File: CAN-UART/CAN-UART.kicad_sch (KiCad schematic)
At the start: 15 parts, among them J1 Conn_01x06, P1 USB_C_Plug_USB2.0, U1 AP2112K-3.3, U2 SN65HVD230, U3 ESP32-C3, U4 AT45DB161D-SU

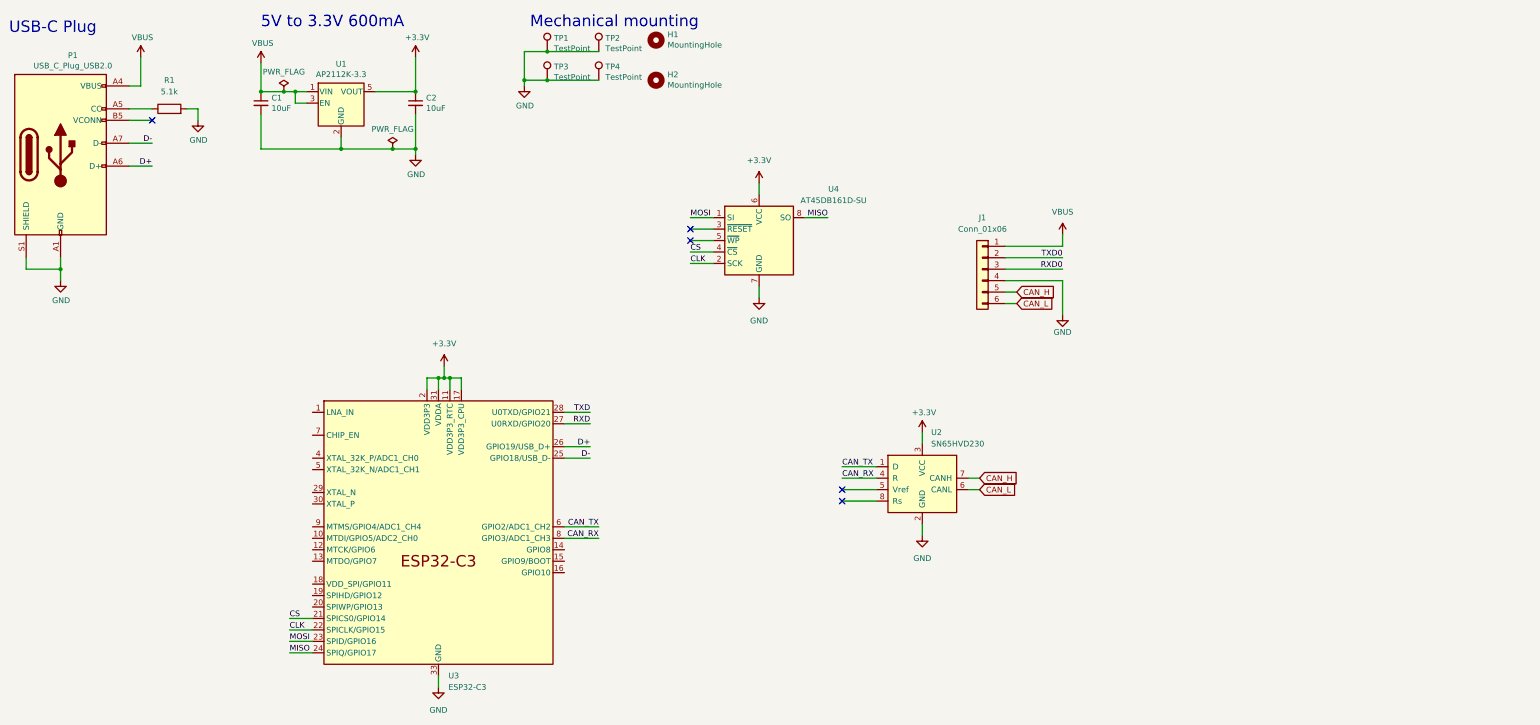
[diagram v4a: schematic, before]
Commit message: Added Power Cap
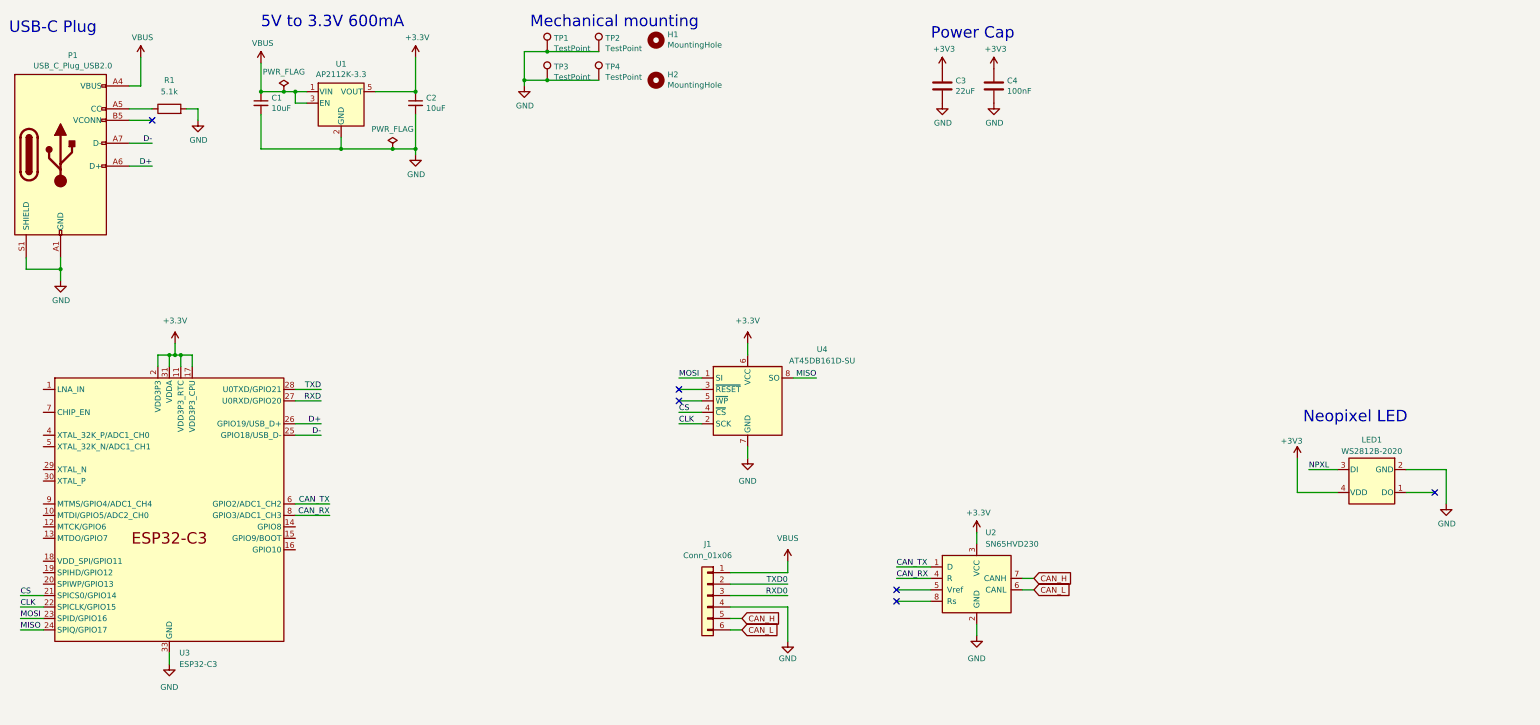
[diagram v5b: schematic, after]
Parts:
- added C3: 22uF, Capacitor_SMD:C_0402_1005Metric_Pad0.74x0.62mm_HandSolder, symbol Device:C
- added C4: 100nF, Capacitor_SMD:C_0402_1005Metric_Pad0.74x0.62mm_HandSolder, symbol Device:C
- added LED1: WS2812B-2020, _mykicadlib:LED-SMD_4P-L2.0-W2.0-TL_WS2812B-2020, symbol _mykicadlib:WS2812B-2020
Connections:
- net +3V3: now also C3.1, C4.1, LED1.4 (VDD)
- net GND: now also C3.2, C4.2, LED1.2 (GND)
- new net NPXL: LED1.3 (DI)
- no-connect marks 5 -> 6
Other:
- note added: "Neopixel LED"
- note added: "Power Cap"
- moved on the sheet: J1, U2, U3, U4

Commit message: Added NeoPixel LED
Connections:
- net NPXL: now also U3.14 (GPIO8)
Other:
- moved on the sheet: LED1
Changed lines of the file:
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@@
   (no_connect (at 57.15 39.37))
   (no_connect (at 173.99 99.06))
-  (no_connect (at 341.63 121.92))
+  (no_connect (at 254 109.22))
   (no_connect (at 222.25 143.51))
   (no_connect (at 173.99 101.6))
-  (wire (pts (xy 311.15 121.92) (xy 320.04 121.92))
+  (wire (pts (xy 223.52 109.22) (xy 232.41 109.22))
     (stroke (width 0) (type default))
   )
@@
     (stroke (width 0) (type default))
   )
-  (wire (pts (xy 341.63 121.92) (xy 335.28 121.92))
+  (wire (pts (xy 254 109.22) (xy 247.65 109.22))
     (stroke (width 0) (type default))
   )
@@
     (stroke (width 0) (type default))
   )
-  (wire (pts (xy 311.15 114.3) (xy 311.15 121.92))
+  (wire (pts (xy 223.52 101.6) (xy 223.52 109.22))
     (stroke (width 0) (type default))
   )
@@
     (stroke (width 0) (type default))
   )
-  (wire (pts (xy 313.69 116.84) (xy 320.04 116.84))
+  (wire (pts (xy 226.06 104.14) (xy 232.41 104.14))
     (stroke (width 0) (type default))
   )
@@
     (stroke (width 0) (type default))
   )
-  (wire (pts (xy 344.17 124.46) (xy 344.17 116.84))
+  (wire (pts (xy 256.54 111.76) (xy 256.54 104.14))
     (stroke (width 0) (type default))
   )
@@
     (stroke (width 0) (type default))
   )
-  (wire (pts (xy 335.28 116.84) (xy 344.17 116.84))
+  (wire (pts (xy 247.65 104.14) (xy 256.54 104.14))
+    (stroke (width 0) (type default))
+  )
+  (wire (pts (xy 96.52 129.54) (xy 88.9 129.54))
     (stroke (width 0) (type default))
   )
@@
     (effects (font (size 2.54 2.54)) (justify left bottom))
   )
-  (text "Neopixel LED" (at 312.42 106.68 0)
+  (text "Neopixel LED" (at 224.79 93.98 0)
     (effects (font (size 2.54 2.54)) (justify left bottom))
   )
@@
     (effects (font (size 1.27 1.27)) (justify right bottom))
   )
-  (label "NPXL" (at 313.69 116.84 0) (fields_autoplaced)
+  (label "NPXL" (at 226.06 104.14 0) (fields_autoplaced)
     (effects (font (size 1.27 1.27)) (justify left bottom))
   )
@@
   )
   (label "TXD" (at 94.615 99.06 180) (fields_autoplaced)
+    (effects (font (size 1.27 1.27)) (justify right bottom))
+  )
+  (label "NPXL" (at 96.52 129.54 180) (fields_autoplaced)
     (effects (font (size 1.27 1.27)) (justify right bottom))
   )
@@
     )
   )
-  (symbol (lib_id "_mykicadlib:WS2812B-2020") (at 327.66 119.38 0) (unit 1)
+  (symbol (lib_id "_mykicadlib:WS2812B-2020") (at 240.03 106.68 0) (unit 1)
     (in_bom yes) (on_board yes) (dnp no) (fields_autoplaced)
-    (property "Reference" "LED1" (at 327.66 110.236 0)
-      (effects (font (size 1.27 1.27)))
-    )
-    (property "Value" "WS2812B-2020" (at 327.66 112.776 0)
-      (effects (font (size 1.27 1.27)))
-    )
-    (property "Footprint" "_mykicadlib:LED-SMD_4P-L2.0-W2.0-TL_WS2812B-2020" (at 327.66 128.27 0)
-      (effects (font (size 1.27 1.27)) hide)
-    )
-    (property "Datasheet" "https://datasheet.lcsc.com/lcsc/2012110135_Worldsemi-WS2812B-2020_C965555.pdf" (at 327.66 130.81 0)
-      (effects (font (size 1.27 1.27)) hide)
-    )
-    (property "Manufacturer" "worldsemi" (at 327.66 133.35 0)
-      (effects (font (size 1.27 1.27)) hide)
-    )
-    (property "LCSC Part" "C965555" (at 327.66 135.89 0)
-      (effects (font (size 1.27 1.27)) hide)
-    )
-    (property "JLC Part" "Extended Part" (at 327.66 138.43 0)
-      (effects (font (size 1.27 1.27)) hide)
-    )
-    (property "LCSC#" "C965555" (at 334.01 130.81 0)
-      (effects (font (size 1.27 1.27)) hide)
-    )
-    (property "Part#" "WS2812B-2020" (at 336.55 133.35 0)
-      (effects (font (size 1.27 1.27)) hide)
-    )
-    (property "MPN" "C965555" (at 327.66 135.89 0)
+    (property "Reference" "LED1" (at 240.03 97.536 0)
+      (effects (font (size 1.27 1.27)))
+    )
+    (property "Value" "WS2812B-2020" (at 240.03 100.076 0)
+      (effects (font (size 1.27 1.27)))
+    )
+    (property "Footprint" "_mykicadlib:LED-SMD_4P-L2.0-W2.0-TL_WS2812B-2020" (at 240.03 115.57 0)
+      (effects (font (size 1.27 1.27)) hide)
+    )
+    (property "Datasheet" "https://datasheet.lcsc.com/lcsc/2012110135_Worldsemi-WS2812B-2020_C965555.pdf" (at 240.03 118.11 0)
+      (effects (font (size 1.27 1.27)) hide)
+    )
+    (property "Manufacturer" "worldsemi" (at 240.03 120.65 0)
+      (effects (font (size 1.27 1.27)) hide)
+    )
+    (property "LCSC Part" "C965555" (at 240.03 123.19 0)
+      (effects (font (size 1.27 1.27)) hide)
+    )
+    (property "JLC Part" "Extended Part" (at 240.03 125.73 0)
+      (effects (font (size 1.27 1.27)) hide)
+    )
+    (property "LCSC#" "C965555" (at 246.38 118.11 0)
+      (effects (font (size 1.27 1.27)) hide)
+    )
+    (property "Part#" "WS2812B-2020" (at 248.92 120.65 0)
+      (effects (font (size 1.27 1.27)) hide)
+    )
+    (property "MPN" "C965555" (at 240.03 123.19 0)
       (effects (font (size 1.27 1.27)) hide)
     )
@@
     )
   )
-  (symbol (lib_id "power:GND") (at 344.17 124.46 0) (unit 1)
-    (in_bom yes) (on_board yes) (dnp no)
-    (property "Reference" "#PWR020" (at 344.17 130.81 0)
-      (effects (font (size 1.27 1.27)) hide)
-    )
-    (property "Value" "GND" (at 344.297 128.8542 0)
-      (effects (font (size 1.27 1.27)))
-    )
-    (property "Footprint" "" (at 344.17 124.46 0)
-      (effects (font (size 1.27 1.27)) hide)
-    )
-    (property "Datasheet" "" (at 344.17 124.46 0)
+  (symbol (lib_id "power:GND") (at 256.54 111.76 0) (unit 1)
+    (in_bom yes) (on_board yes) (dnp no)
+    (property "Reference" "#PWR020" (at 256.54 118.11 0)
+      (effects (font (size 1.27 1.27)) hide)
+    )
+    (property "Value" "GND" (at 256.667 116.1542 0)
+      (effects (font (size 1.27 1.27)))
+    )
+    (property "Footprint" "" (at 256.54 111.76 0)
+      (effects (font (size 1.27 1.27)) hide)
+    )
+    (property "Datasheet" "" (at 256.54 111.76 0)
       (effects (font (size 1.27 1.27)) hide)
     )
@@
     )
   )
-  (symbol (lib_id "power:+3V3") (at 311.15 114.3 0) (unit 1)
-    (in_bom yes) (on_board yes) (dnp no)
-    (property "Reference" "#PWR019" (at 311.15 118.11 0)
-      (effects (font (size 1.27 1.27)) hide)
-    )
-    (property "Value" "+3V3" (at 309.88 110.49 0)
-      (effects (font (size 1.27 1.27)))
-    )
-    (property "Footprint" "" (at 311.15 114.3 0)
-      (effects (font (size 1.27 1.27)) hide)
-    )
-    (property "Datasheet" "" (at 311.15 114.3 0)
-      (effects (font (size 1.27 1.27)) hide)
-    )
+  (symbol (lib_id "power:+3V3") (at 223.52 101.6 0) (unit 1)
+    (in_bom yes) (on_board yes) (dnp no)
+    (property "Reference" "#PWR019" (at 223.52 105.41 0)
+      (effects (font (size 1.27 1.27)) hide)
+    )
+    (property "Value" "+3V3" (at 222.25 97.79 0)
+      (effects (font (size 1.27 1.27)))
+    )
+    (property "Footprint" "" (at 223.52 101.6 0)
+      (effects (font (size 1.27 1.27)) hide)
+    )
+    (property "Datasheet" "" (at 223.52 101.6 0)
+      (effects (font (size 1.27 1.27)) hide)
+    )

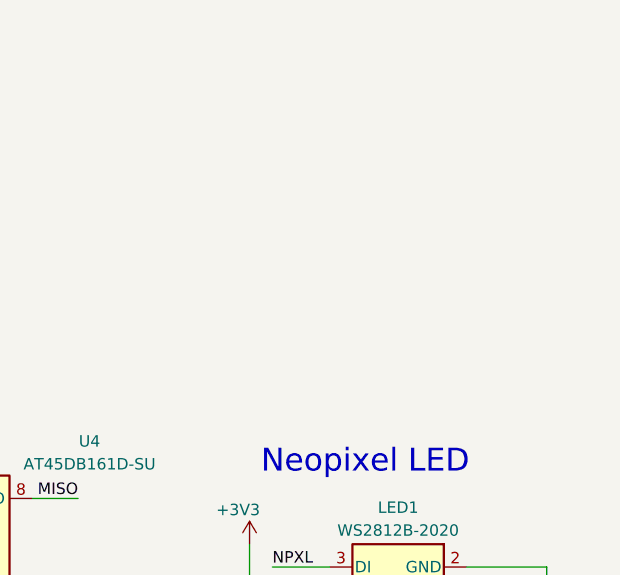
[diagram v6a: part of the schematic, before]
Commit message: Added QWiiC Connector
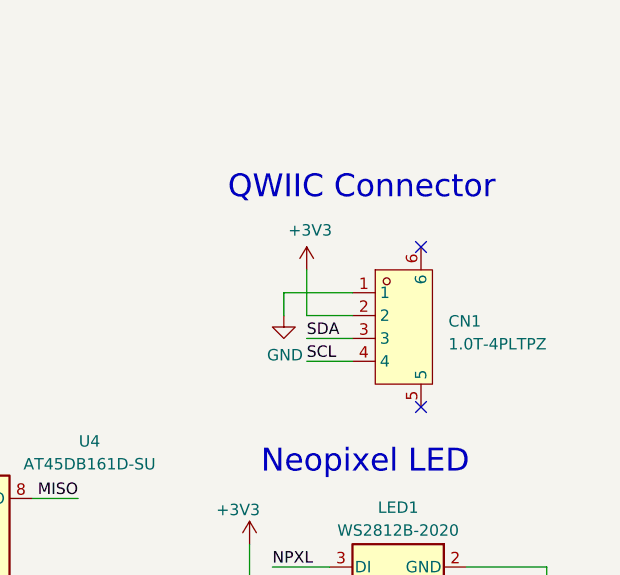
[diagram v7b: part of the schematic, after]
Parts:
- added CN1: 1.0T-4PLTPZ, _mykicadlib:FPC-SMD_4P-P1.00_1.0T-4PLTPZ, symbol _mykicadlib:QWIIC_1.0T-4PLTPZ
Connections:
- net +3V3: now also CN1.2
- net GND: now also CN1.1
- new net SCL: CN1.4
- new net SDA: CN1.3
- no-connect marks 6 -> 8
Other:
- note added: "QWIIC Connector"
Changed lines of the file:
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@@
   (no_connect (at 222.25 146.05))
   (no_connect (at 57.15 39.37))
+  (no_connect (at 242.57 68.58))
+  (no_connect (at 242.57 86.36))
   (no_connect (at 173.99 99.06))
   (no_connect (at 254 109.22))
@@
     (stroke (width 0) (type default))
   )
+  (wire (pts (xy 229.87 76.2) (xy 234.95 76.2))
+    (stroke (width 0) (type default))
+  )
   (wire (pts (xy 96.52 124.46) (xy 88.9 124.46))
     (stroke (width 0) (type default))
@@
     (stroke (width 0) (type default))
   )
+  (wire (pts (xy 229.87 71.12) (xy 229.87 76.2))
+    (stroke (width 0) (type default))
+  )
   (wire (pts (xy 250.19 143.51) (xy 252.73 143.51))
     (stroke (width 0) (type default))
@@
     (stroke (width 0) (type default))
   )
+  (wire (pts (xy 229.87 78.74) (xy 234.95 78.74))
+    (stroke (width 0) (type default))
+  )
   (wire (pts (xy 222.25 146.05) (xy 229.87 146.05))
     (stroke (width 0) (type default))
@@
     (stroke (width 0) (type default))
   )
+  (wire (pts (xy 227.33 73.66) (xy 227.33 76.2))
+    (stroke (width 0) (type default))
+  )
   (wire (pts (xy 199.39 96.52) (xy 204.47 96.52))
     (stroke (width 0) (type default))
@@
     (stroke (width 0) (type default))
   )
+  (wire (pts (xy 227.33 73.66) (xy 234.95 73.66))
+    (stroke (width 0) (type default))
+  )
   (wire (pts (xy 88.9 33.02) (xy 91.44 33.02))
     (stroke (width 0) (type default))
@@
   )
   (wire (pts (xy 81.28 26.67) (xy 81.28 33.02))
+    (stroke (width 0) (type default))
+  )
+  (wire (pts (xy 229.87 81.28) (xy 234.95 81.28))
     (stroke (width 0) (type default))
   )
@@
     (effects (font (size 2.54 2.54)) (justify left bottom))
   )
+  (text "QWIIC Connector" (at 221.107 63.5 0)
+    (effects (font (size 2.54 2.54)) (justify left bottom))
+  )
   (text "Power Cap" (at 229.87 21.59 0)
     (effects (font (size 2.54 2.54)) (justify left bottom))
@@
     (effects (font (size 1.27 1.27)) (justify left bottom))
   )
+  (label "SCL" (at 229.87 81.28 0) (fields_autoplaced)
+    (effects (font (size 1.27 1.27)) (justify left bottom))
+  )
   (label "CS" (at 173.99 104.14 0) (fields_autoplaced)
     (effects (font (size 1.27 1.27)) (justify left bottom))
@@
   (label "D-" (at 57.15 44.45 180) (fields_autoplaced)
     (effects (font (size 1.27 1.27)) (justify right bottom))
+  )
+  (label "SDA" (at 229.87 78.74 0) (fields_autoplaced)
+    (effects (font (size 1.27 1.27)) (justify left bottom))
   )
   (label "CAN_TX" (at 96.52 124.46 180) (fields_autoplaced)
@@
         (path "/21020eba-b649-4135-9bee-384d0a5cab58"
           (reference "#PWR0101") (unit 1)
+        )
+      )
+    )
+  )
+  (symbol (lib_id "_mykicadlib:QWIIC_1.0T-4PLTPZ") (at 238.76 77.47 0) (unit 1)
+    (in_bom yes) (on_board yes) (dnp no) (fields_autoplaced)
+    (property "Reference" "CN1" (at 245.618 76.835 0)
+      (effects (font (size 1.27 1.27)) (justify left))
+    )
+    (property "Value" "1.0T-4PLTPZ" (at 245.618 79.375 0)
+      (effects (font (size 1.27 1.27)) (justify left))
+    )
+    (property "Footprint" "_mykicadlib:FPC-SMD_4P-P1.00_1.0T-4PLTPZ" (at 238.76 93.98 0)
+      (effects (font (size 1.27 1.27)) hide)
+    )
+    (property "Datasheet" "" (at 238.76 77.47 0)
+      (effects (font (size 1.27 1.27)) hide)
+    )
+    (property "MPN" "C2974722" (at 238.76 99.06 0)
+      (effects (font (size 1.27 1.27)) hide)
+    )
+    (pin "1")
+    (pin "2")
+    (pin "3")
+    (pin "4")
+    (pin "5")
+    (pin "6")
+    (instances
+      (project "CAN-UART"
+        (path "/21020eba-b649-4135-9bee-384d0a5cab58"
+          (reference "CN1") (unit 1)
+        )
+      )
+      (project "ESP32-S3-Expansion"
+        (path "/fb4ba2fe-1d6d-4cc7-9c97-5f7d41344916"
+          (reference "CN1") (unit 1)
         )
       )
@@
     )
   )
+  (symbol (lib_id "power:+3V3") (at 229.87 71.12 0) (unit 1)
+    (in_bom yes) (on_board yes) (dnp no)
+    (property "Reference" "#PWR022" (at 229.87 74.93 0)
+      (effects (font (size 1.27 1.27)) hide)
+    )
+    (property "Value" "+3V3" (at 230.251 66.7258 0)
+      (effects (font (size 1.27 1.27)))
+    )
+    (property "Footprint" "" (at 229.87 71.12 0)
+      (effects (font (size 1.27 1.27)) hide)
+    )
+    (property "Datasheet" "" (at 229.87 71.12 0)
+      (effects (font (size 1.27 1.27)) hide)
+    )
+    (pin "1")
+    (instances
+      (project "CAN-UART"
+        (path "/21020eba-b649-4135-9bee-384d0a5cab58"
+          (reference "#PWR022") (unit 1)
+        )
+      )
+      (project "Andromeda-mkII"
+        (path "/828656dd-6a21-4917-a16e-ca9e39bf37f8"
+          (reference "#PWR?") (unit 1)
+        )
+      )
+      (project "Andromeda32-S3"
+        (path "/be31e571-bd5d-4296-830e-05334f237a7a"
+          (reference "#PWR026") (unit 1)
+        )
+      )
+      (project "ESP32-S3-Expansion"
+        (path "/fb4ba2fe-1d6d-4cc7-9c97-5f7d41344916"
+          (reference "#PWR025") (unit 1)
+        )
+      )
+    )
+  )
   (symbol (lib_id "Memory_Flash:AT45DB161D-SU") (at 189.23 101.6 0) (unit 1)
     (in_bom yes) (on_board yes) (dnp no)
@@
         )
       )
+    )
+  )
+  (symbol (lib_id "power:GND") (at 227.33 76.2 0) (unit 1)
+    (in_bom yes) (on_board yes) (dnp no)
+    (property "Reference" "#PWR021" (at 227.33 82.55 0)
+      (effects (font (size 1.27 1.27)) hide)
+    )
+    (property "Value" "GND" (at 227.457 80.5942 0)
+      (effects (font (size 1.27 1.27)))
+    )
+    (property "Footprint" "" (at 227.33 76.2 0)
+      (effects (font (size 1.27 1.27)) hide)
+    )
+    (property "Datasheet" "" (at 227.33 76.2 0)
+      (effects (font (size 1.27 1.27)) hide)
+    )
+    (pin "1")
+    (instances
+      (project "CAN-UART"
+        (path "/21020eba-b649-4135-9bee-384d0a5cab58"
+          (reference "#PWR021") (unit 1)
+        )
+      )
+      (project "Andromeda-mkII"
+        (path "/828656dd-6a21-4917-a16e-ca9e39bf37f8"
+          (reference "#PWR?") (unit 1)
+        )
+      )
+      (project "Andromeda32-S3"
+        (path "/be31e571-bd5d-4296-830e-05334f237a7a"
+          (reference "#PWR028") (unit 1)
+        )
+      )
+      (project "ESP32-S3-Expansion"
+        (path "/fb4ba2fe-1d6d-4cc7-9c97-5f7d41344916"
+          (reference "#PWR026") (unit 1)
+        )
+      )
